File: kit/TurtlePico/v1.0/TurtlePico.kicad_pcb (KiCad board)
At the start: 2 copper layers, 63.5 x 69.3 mm, 46 parts, among them IC1 DRV8835DSSR, J1 USB-C, J10 LMotor, J11 Micro_SD, J12 FR_ESC, J13 FL_ESC, J14 RR_ESC, J15 RL_ESC, J2 AudioJack3, J3 LED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

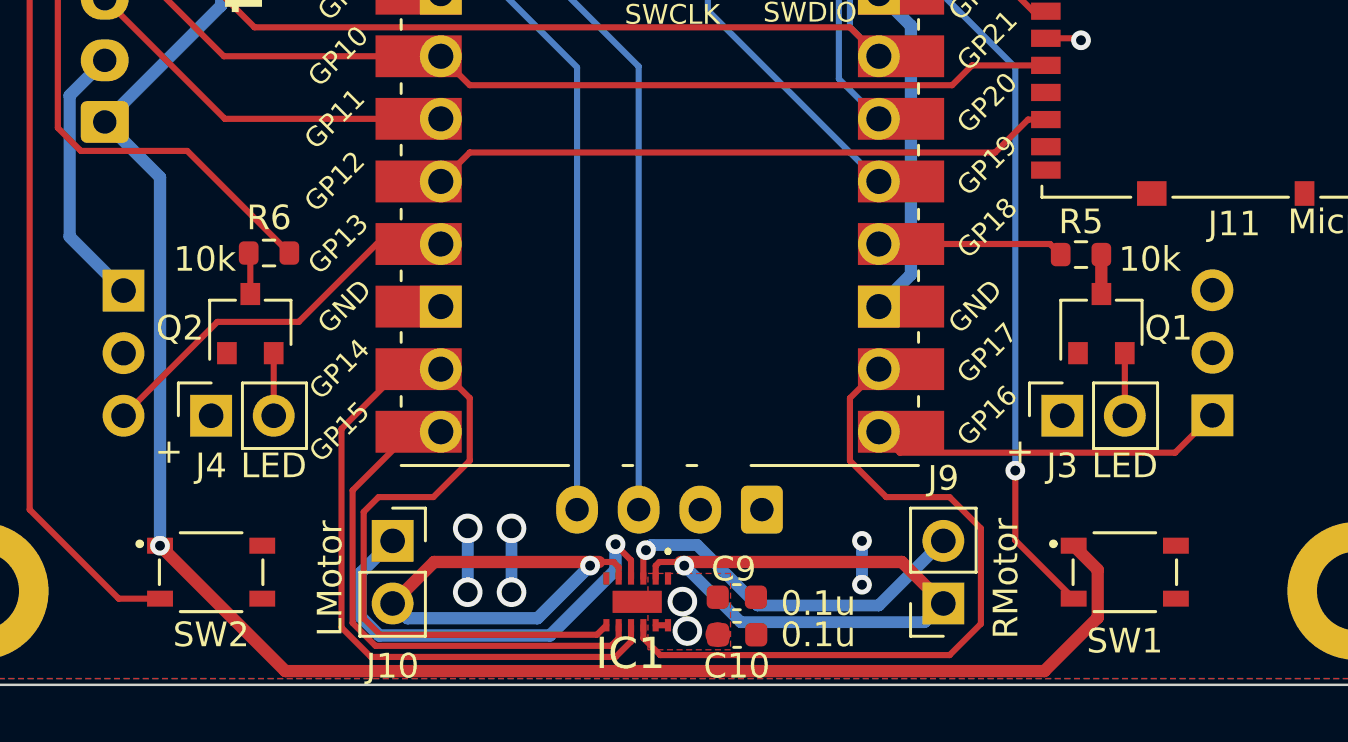
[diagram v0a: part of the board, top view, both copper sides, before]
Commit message: change BJT and some design
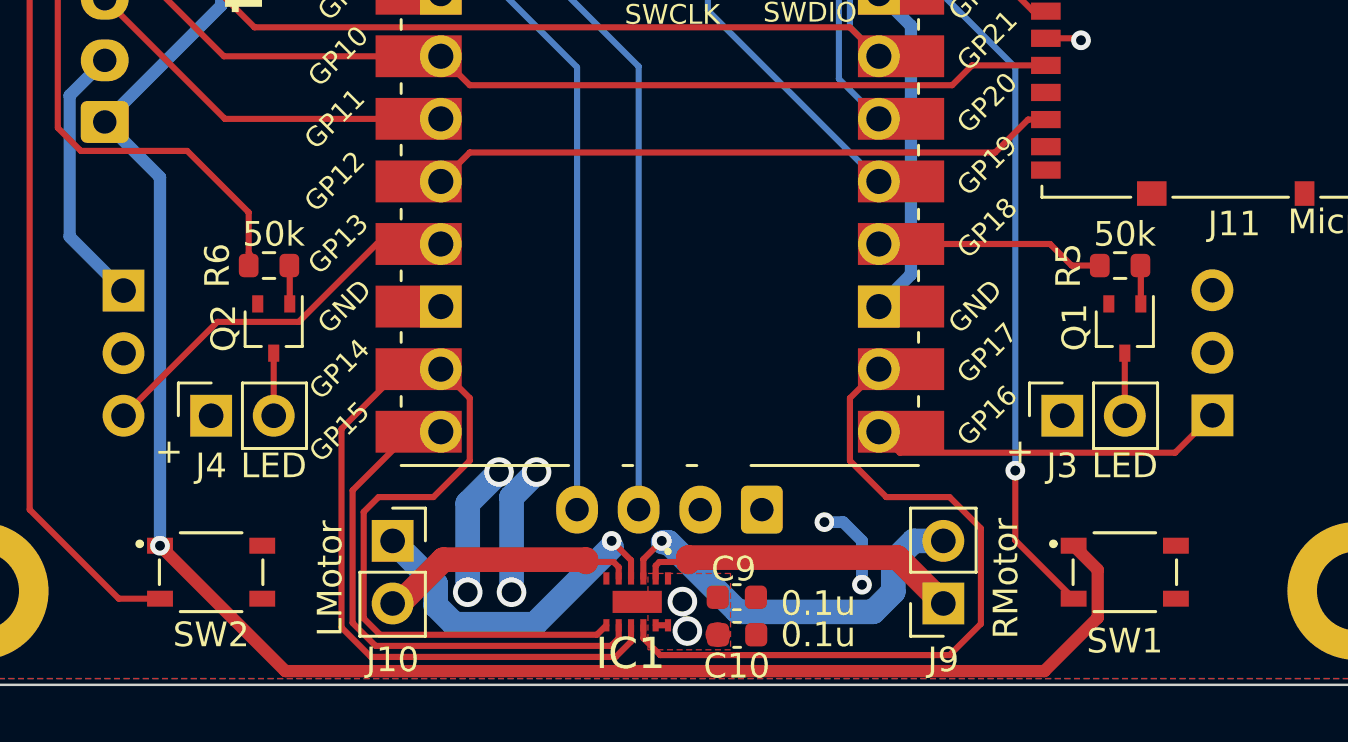
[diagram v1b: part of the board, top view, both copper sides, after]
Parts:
- Q1, Q2: value 2SC1815 -> 2SC4213; footprint Package_TO_SOT_SMD:SC-59 -> Package_TO_SOT_SMD:SOT-323_SC-70
- R5, R6: value 10k -> 50k
- moved R5 1.65 mm to (164.1, 113.3)
- moved Q2 0.97 mm to (129.8, 115.8), turned to -90 degrees
- moved Q1 0.97 mm to (164.3, 115.8), turned to -90 degrees
- moved R6 0.51 mm to (129.6, 113.3), turned to 180 degrees
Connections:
- Q1 pad 1: GND -> Net-(Q1-B)
- Q1 pad 2: Net-(J3-Pin_2) -> GND
- Q1 pad 3: Net-(Q1-B) -> Net-(J3-Pin_2)
- Q2 pad 1: GND -> Net-(Q2-B)
- Q2 pad 2: Net-(J4-Pin_2) -> GND
- Q2 pad 3: Net-(Q2-B) -> Net-(J4-Pin_2)
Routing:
- net Net-(IC1-AOUT1): track 24.7 -> 12.9 mm, vias 1 -> 0
- net Net-(IC1-BOUT2): track 19.6 -> 10.0 mm, vias 1 -> 0
- net GND: track 75.6 -> 82.9 mm
- net Net-(IC1-BOUT1): track 18.5 -> 13.9 mm
- net /GP18: track 7.56 -> 9.33 mm
- net /GP4: track 45.7 -> 45.2 mm
- net Net-(IC1-AOUT2): track 15.7 -> 16.3 mm

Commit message: update v1.1 fix usb
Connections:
- J1 pad A6: Net-(J1-DN2) -> Net-(J1-DP1)
- J1 pad B6: Net-(J1-DN1) -> Net-(J1-DP1)
- J1 pad B7: Net-(J1-DN2) -> Net-(J1-DN1)
- U2 pad TP2: Net-(J1-DN2) -> Net-(J1-DN1)
- U2 pad TP3: Net-(J1-DN1) -> Net-(J1-DP1)
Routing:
- net Net-(J1-DN2): track 34.6 -> 0.00 mm
- net Net-(J1-DP1): track 0.00 -> 28.8 mm
- net Net-(J1-DN1): track 26.9 -> 36.7 mm
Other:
- board text added: "Turtle Pico v1.1"
- board text removed: "Turtle Pico v1.0"

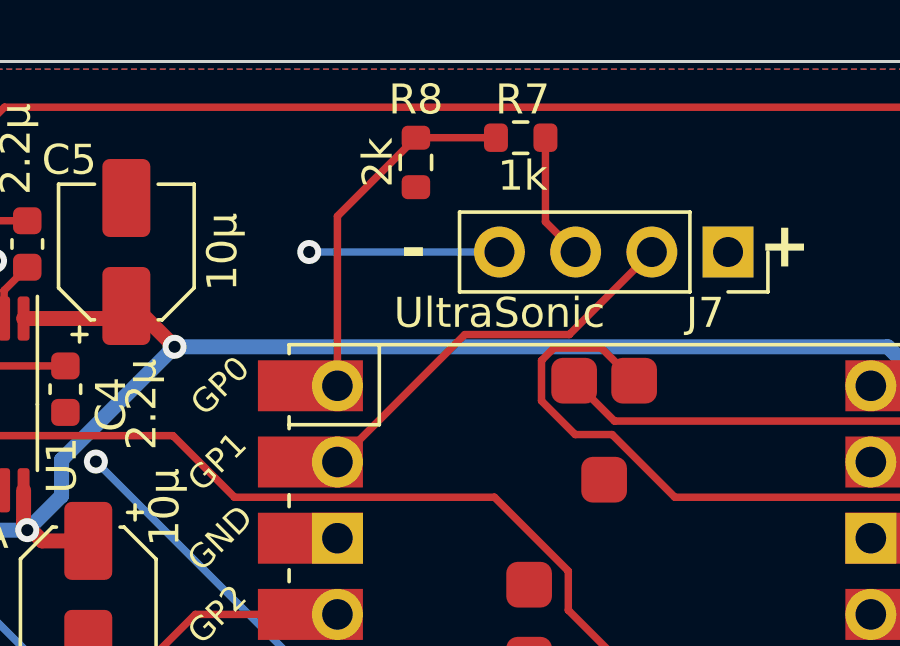
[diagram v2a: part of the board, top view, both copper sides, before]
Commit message: update v.1 change uart and ultrasonic pin
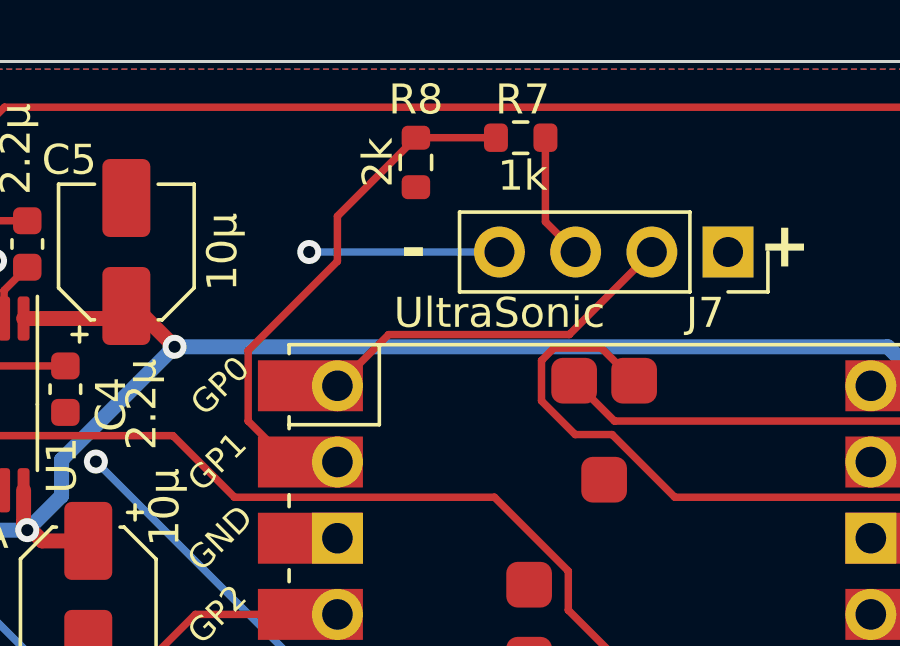
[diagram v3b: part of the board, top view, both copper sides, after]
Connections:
- J7 pad 2: /GP1 -> /GP0
- R7 pad 2: /GP0 -> /GP1
- R8 pad 1: /GP0 -> /GP1
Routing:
- net /GP1: track 13.4 -> 18.0 mm
